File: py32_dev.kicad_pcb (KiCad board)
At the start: 2 copper layers, 68 x 32 mm, 34 parts, among them J1 Board Pwr, J2 Conn_01x18, J3 Conn_01x18, SW1 Usr, SW2 Reset, U1 uA7805, U2 PY32F030K1xT, Y1 24MHz, Y2 32.768KHz

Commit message: Updated README
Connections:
- net Net-(C1-Pad1) renamed /VBUS
- J2 pad 1: VDD -> GND
- J3 pad 1: GND -> VDD
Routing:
- net VDD: track 26.9 -> 0.00 mm, vias 1 -> 0
- net /VBUS: track 14.2 -> 0.00 mm
- added copper zone on F.Cu, net /VBUS

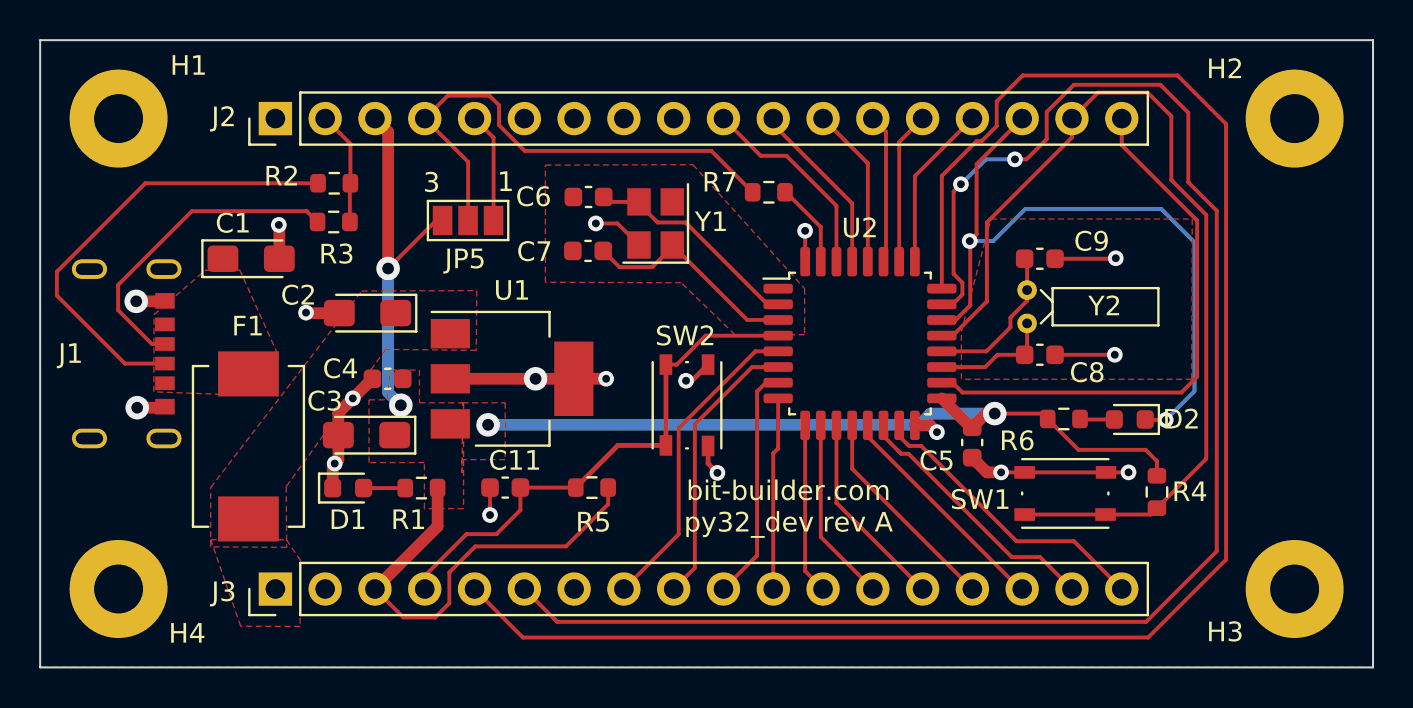
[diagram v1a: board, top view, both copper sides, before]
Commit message: Updated revision to B
Moved fuse slightly away from USB connector on the pcb for more room
to resolder the USB connector pins
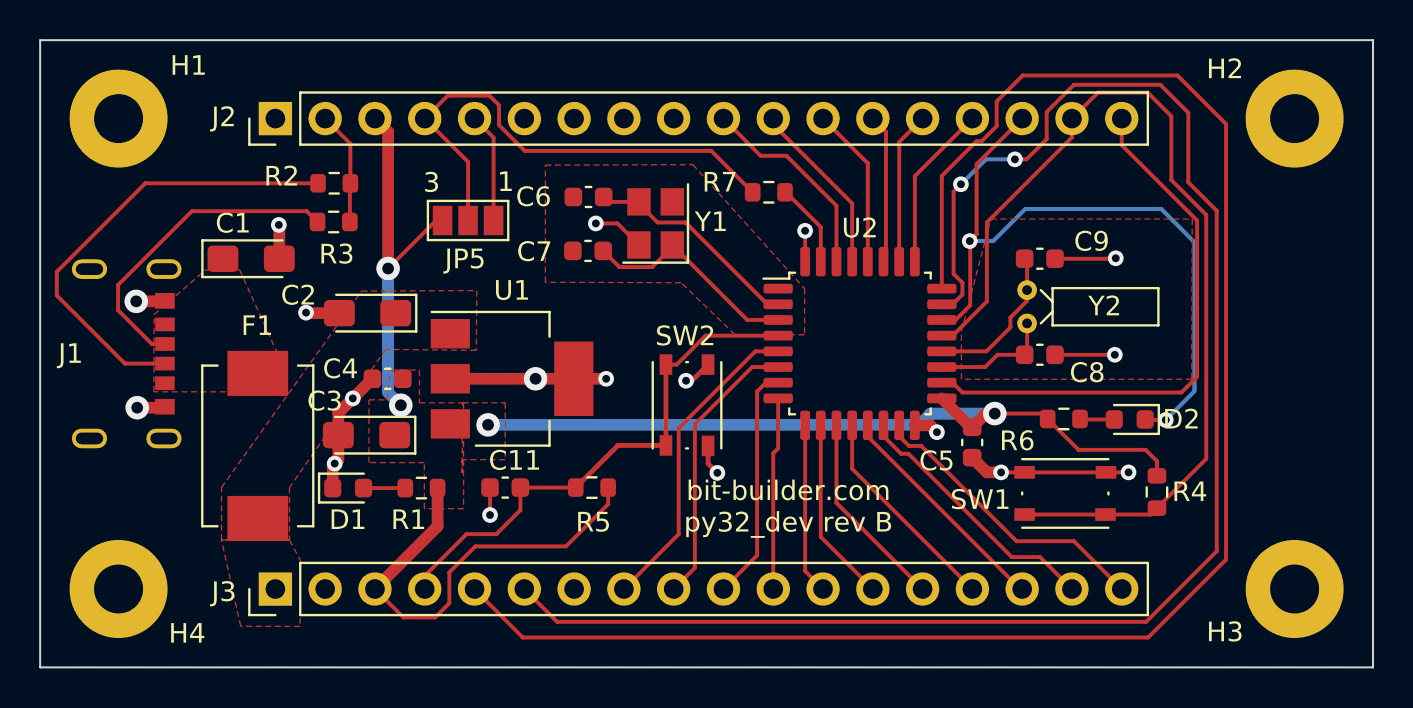
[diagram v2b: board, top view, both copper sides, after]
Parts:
- R2, R3: value R -> 5.1K
- moved F1 0.48 mm to (133.1, 113.7)
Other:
- board text added: "bit-builder.com py32_dev rev B"
- board text removed: "bit-builder.com py32_dev rev A"
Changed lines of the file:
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@@
   (title_block
     (title "py32_dev")
-    (rev "A")
+    (rev "B")
     (company "bit-builder.com")
   )
@@
   )
   (footprint "Fuse:Fuse_Bourns_MF-SM_7.98x5.44mm" (layer "F.Cu")
-    (at 132.625 113.725 -90)
+    (at 133.1 113.7 -90)
     (descr "https://www.bourns.com/docs/Product-Datasheets/mfsm.pdf")
     (tags "bourns ptc resettable fuse polyfuse MF-SM MF-SMHT")
@@
       (effects (font (size 1 1) (thickness 0.15)))
     )
-    (fp_text value "R" (at 0 1.43) (layer "F.Fab")
+    (fp_text value "5.1K" (at 0 1.43) (layer "F.Fab")
       (effects (font (size 1 1) (thickness 0.15)))
     )
@@
       (effects (font (size 1 1) (thickness 0.15)))
     )
-    (fp_text value "R" (at 0 1.43) (layer "F.Fab")
+    (fp_text value "5.1K" (at 0 1.43) (layer "F.Fab")
       (effects (font (size 1 1) (thickness 0.15)))
     )
@@
   )
   (gr_rect (start 122 93) (end 190 125) (layer "Edge.Cuts") (width 0.1) (fill none))
-  (gr_text "bit-builder.com\npy32_dev rev A" (at 160.175 116.8) (layer "F.SilkS")
+  (gr_text "bit-builder.com\npy32_dev rev B" (at 160.175 116.8) (layer "F.SilkS")
     (effects (font (size 1 1) (thickness 0.15)))
   )
@@
         (xy 144.25 108.825)
         (xy 139.625 108.775)
-        (xy 134.55 115.775)
-        (xy 134.575 118.875)
-        (xy 130.7 118.85)
-        (xy 130.7 115.825)
+        (xy 134.72 115.82)
+        (xy 134.72 118.51)
+        (xy 131.25 118.51)
+        (xy 131.25 115.825)
         (xy 138.4 105.8)
       )
@@
         (xy 135.26 122.91)
         (xy 132.23 122.9)
-        (xy 130.7 118.49)
-        (xy 134.57 118.49)
+        (xy 131.25 118.49)
+        (xy 134.72 118.5)
       )
     )
@@
       (pts
         (xy 134.17 109.13)
-        (xy 131.22 109.13)
-        (xy 131.22 111.07)
+        (xy 131.96 109.13)
+        (xy 131.96 110.94)
         (xy 127.8 110.94)
         (xy 127.81 107)

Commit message: Redid user pushbutton to work correctly
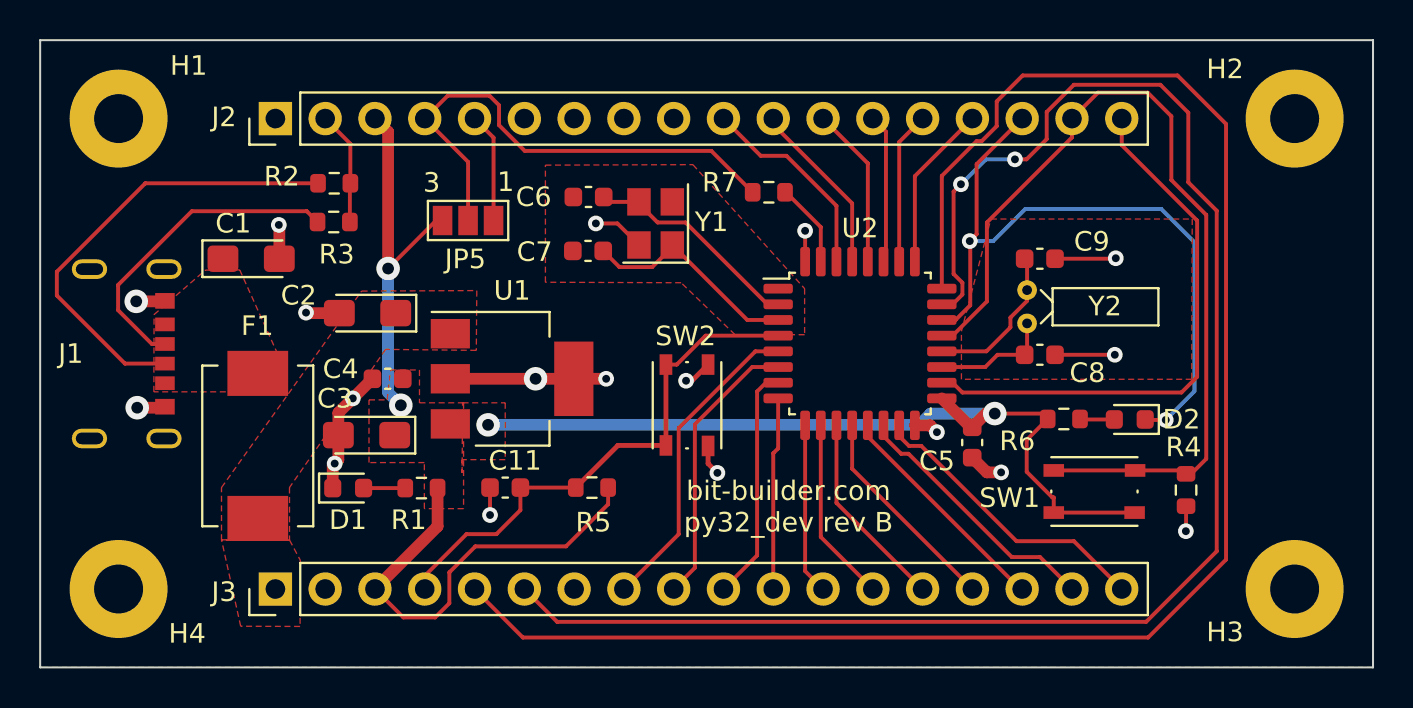
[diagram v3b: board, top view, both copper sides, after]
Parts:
- moved R4 1.49 mm to (180.5, 116.0)
- moved SW1 1.49 mm to (175.8, 116.0)
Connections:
- R4 pad 1: PA11 -> GND
- R4 pad 2: +3.3V -> PA11
- SW1 pad 1: GND -> PA11
- SW1 pad 2: PA11 -> +3.3V
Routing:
- net GND: track 55.7 -> 50.5 mm
- net +3.3V: track 81.9 -> 84.6 mm
- net PA11: track 48.9 -> 46.7 mm

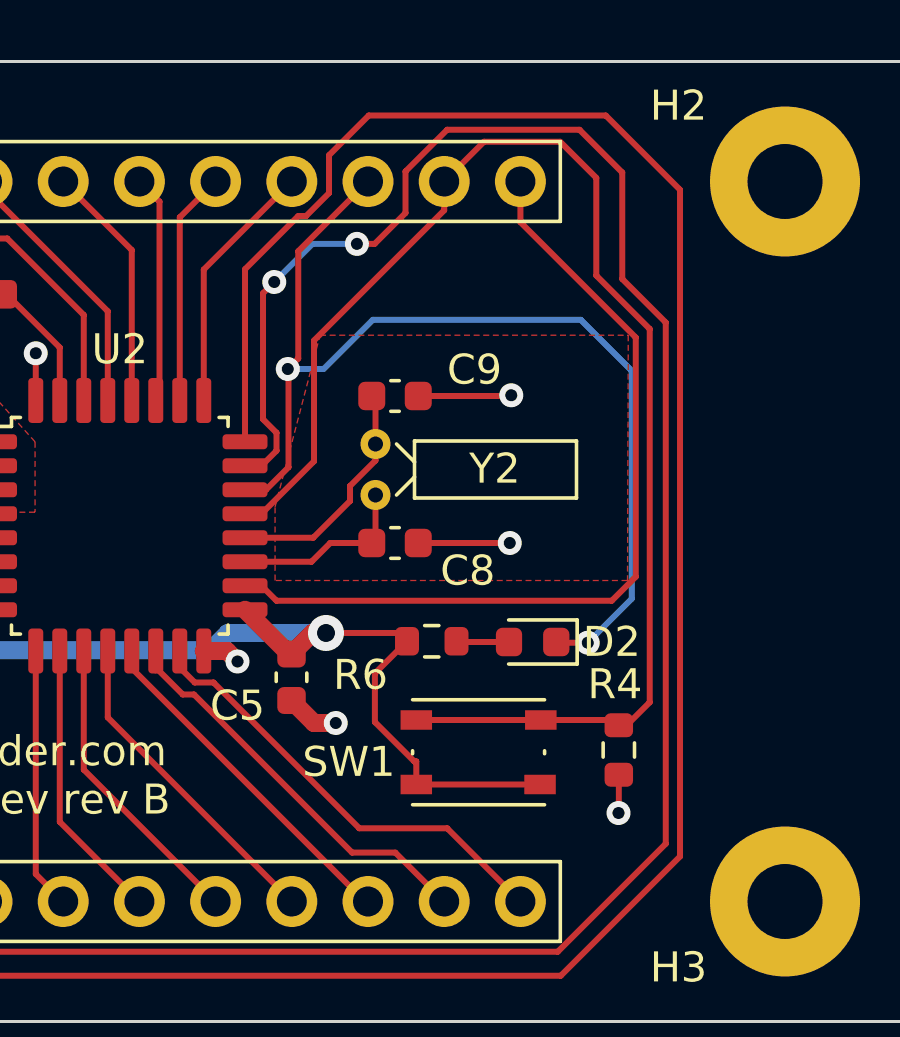
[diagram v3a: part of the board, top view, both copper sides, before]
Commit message: Removed R4, user PB swap, back to rev A config
Added link in README to blink firmware repository and puya32 tech docs
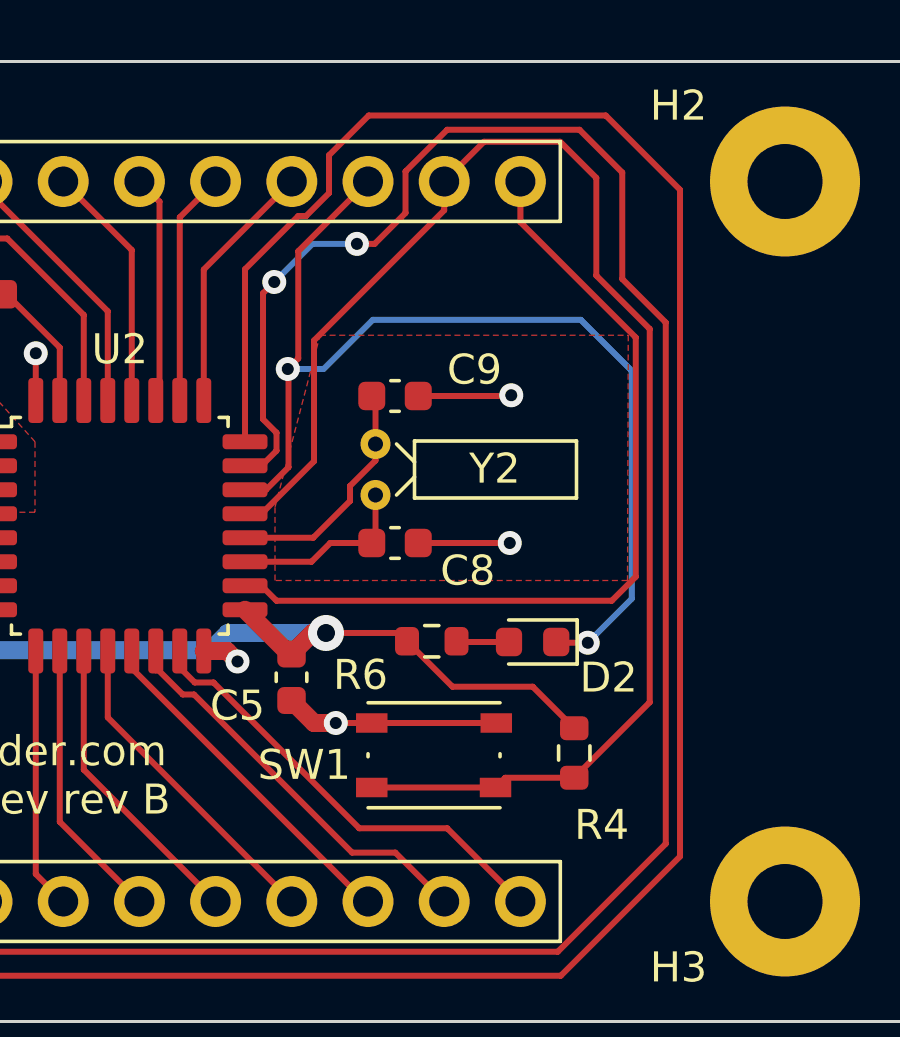
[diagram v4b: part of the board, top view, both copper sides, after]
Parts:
- moved R4 1.49 mm to (179.0, 116.0)
- moved SW1 1.49 mm to (174.3, 116.1)
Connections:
- R4 pad 1: GND -> PA11
- R4 pad 2: PA11 -> +3.3V
- SW1 pad 1: PA11 -> GND
- SW1 pad 2: +3.3V -> PA11
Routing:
- net GND: track 50.5 -> 54.6 mm, vias 18 -> 17
- net +3.3V: track 84.6 -> 81.4 mm
- net PA11: track 46.7 -> 48.9 mm
